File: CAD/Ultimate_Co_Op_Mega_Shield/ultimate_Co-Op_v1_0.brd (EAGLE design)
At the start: 91.1 x 53.3 mm, 50 parts

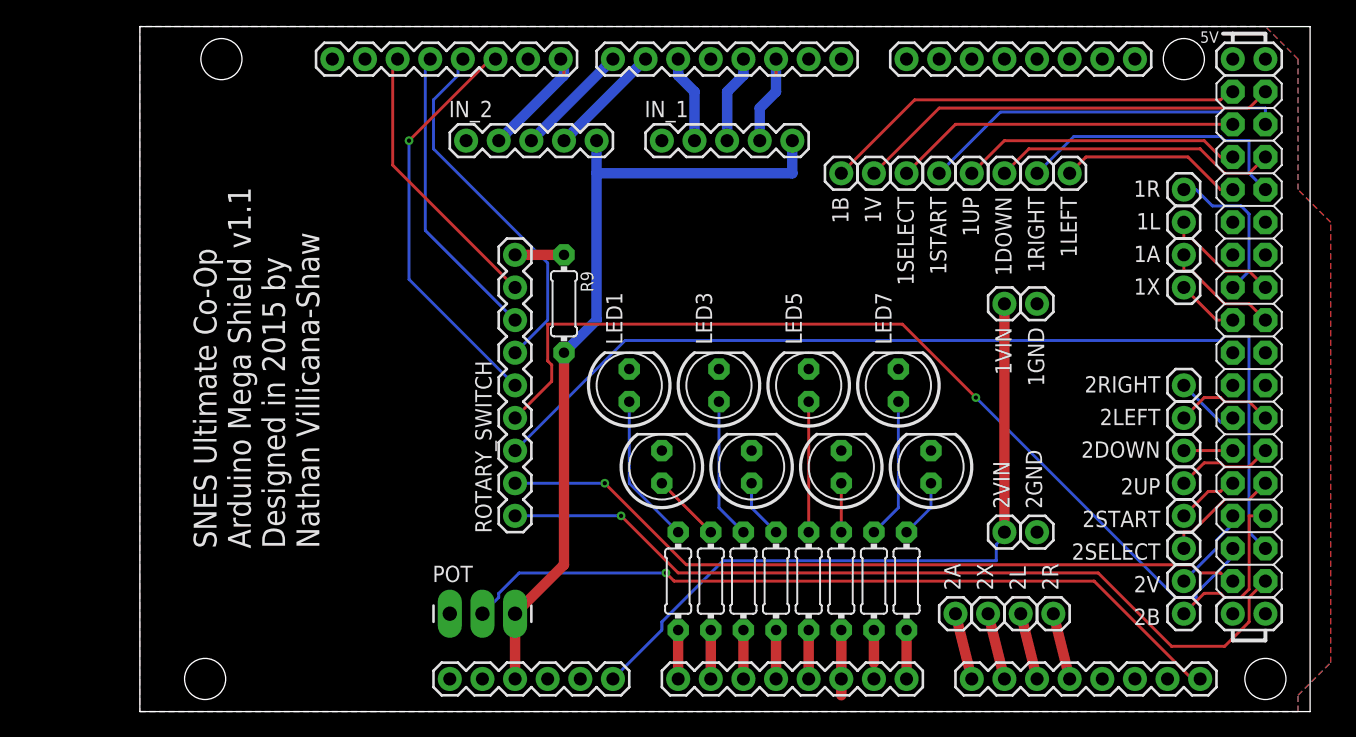
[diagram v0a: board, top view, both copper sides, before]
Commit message: created a 'mini' version of the co-op board
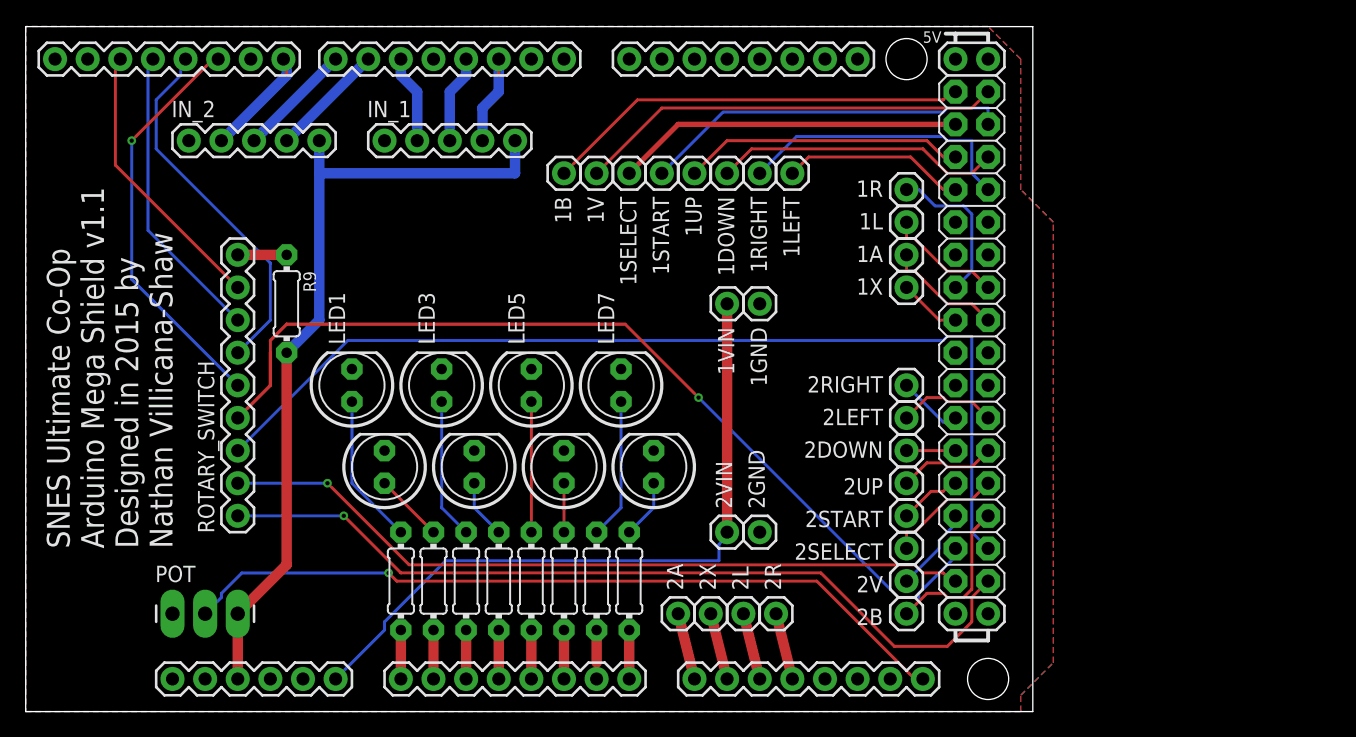
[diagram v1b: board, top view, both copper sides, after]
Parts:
- ARDUINO_MEGA: device SparkFun-Boards:ARDUINO_MEGA -> Nathans-Boards_small_mega:ARDUINO_MEGA
- moved 1A 21.6 mm to (68.6, 35.6)
- moved 1B 21.6 mm to (41.9, 41.9)
- moved 1DOWN 21.6 mm to (54.6, 41.9)
- moved 1L 21.6 mm to (68.6, 38.1)
- moved 1LEFT 21.6 mm to (59.7, 41.9)
- moved 1R 21.6 mm to (68.6, 40.6)
- moved 1START 21.6 mm to (49.5, 41.9)
- moved 1V 21.6 mm to (44.5, 41.9)
- moved 1VIN 21.6 mm to (54.6, 31.8)
- moved 1X 21.6 mm to (68.6, 33.0)
- moved 2A 21.6 mm to (50.8, 7.62)
- moved 2B 21.6 mm to (68.6, 7.62)
- moved 2DOWN 21.6 mm to (68.6, 20.3)
- moved 2LEFT 21.6 mm to (68.6, 22.9)
- moved 2R 21.6 mm to (58.4, 7.62)
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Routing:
- net LED6: track 5.08 -> 3.81 mm
- net OUT2_B: track 13.1 -> 12.4 mm
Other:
- board size 91.1 x 53.3 mm -> 78.4 x 53.3 mm
